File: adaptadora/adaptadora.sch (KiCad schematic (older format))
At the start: 27 parts, among them J1 Conn_Coaxial, J10 Conn_Coaxial, J11 Conn_Coaxial, J2 Conn_Coaxial, J3 Conn_Coaxial, J4 Conn_Coaxial, J5 Conn_02x20_Odd_Even, J6 Conn_01x02, J7 Conn_02x20_Odd_Even, J8 Conn_01x04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

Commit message: esq y pcb work in progress
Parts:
- added H1, H2, H3, H4, H5: MountingHole, MountingHole:MountingHole_3.2mm_M3_Pad, symbol Mechanical:MountingHole
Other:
- moved on the sheet: D1, D2, J1, J2, J3, J4, J7, JP1, JP2, R1, R2, RV1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

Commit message: mejorando BOM - work in progress
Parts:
- U25: Descripción (inglés) Dual 2.7-V High Slew Rate Rail-To-Rail Output Operational A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 -> General Purpose Amplifier 2 Circuit Rail-to-Rail 8-SOIC; Enlace https://www.digikey.com/product-detail/en/texas-instruments/TLV2772IDR/296-1902-1-ND/405014?utm_source=snapeda&utm_medium=aggregator&utm_campaign=symbol -> https://www.digikey.com/product-detail/en/texas-instruments/TLV2772IDR/296-1902-2-ND/374332; Número de Parte (Digi-Key) 296-1902-1-ND -> 296-1902-2-ND; Número de parte (Digi-Key) (none) -> 296-1902-2-ND
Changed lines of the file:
@@
 F 3 "http://www.ti.com/lit/ds/symlink/tlv2772.pdf" H 8950 1150 50  0001 L BNN
 F 4 "Texas Instruments" H 8950 1150 50  0001 L BNN "Fabricante"
-F 5 "Dual 2.7-V High Slew Rate Rail-To-Rail Output Operational Amplifier 8-SOIC -40 to 125" H 8950 1150 50  0001 L BNN "Descripción (inglés)"
-F 6 "296-1902-1-ND" H 8950 1150 50  0001 L BNN "Número de Parte (Digi-Key)"
-F 7 "https://www.digikey.com/product-detail/en/texas-instruments/TLV2772IDR/296-1902-1-ND/405014?utm_source=snapeda&utm_medium=aggregator&utm_campaign=symbol" H 8950 1150 50  0001 L BNN "Enlace"
+F 5 "General Purpose Amplifier 2 Circuit Rail-to-Rail 8-SOIC" H 8950 1150 50  0001 L BNN "Descripción (inglés)"
+F 6 "296-1902-2-ND" H 8950 1150 50  0001 L BNN "Número de Parte (Digi-Key)"
+F 7 "https://www.digikey.com/product-detail/en/texas-instruments/TLV2772IDR/296-1902-2-ND/374332" H 8950 1150 50  0001 L BNN "Enlace"
+F 8 "296-1902-2-ND" H 8950 1600 50  0001 C CNN "Número de parte (Digi-Key)"
+F 9 "" H 8950 1600 50  0001 C CNN "Campo9"
+F 10 "" H 8950 1600 50  0001 C CNN "Campo10"
 	1    8950 1600
 	1    0    0    -1
@@
 $EndComp
 $Comp
-L power:GND #PWR04
-U 1 1 5DAF1F2B
-P 5150 4950
-F 0 "#PWR04" H 5150 4700 50  0001 C CNN
-F 1 "GND" H 5155 4777 50  0000 C CNN
-F 2 "" H 5150 4950 50  0001 C CNN
-F 3 "" H 5150 4950 50  0001 C CNN
-	1    5150 4950
-	1    0    0    -1
-$EndComp
-$Comp
 L power:+5V #PWR05
 U 1 1 5DAF2B68
@@
 Wire Wire Line
 	5400 5100 5600 5100
-Text GLabel 5600 5300 0    50   Input ~ 0
-DAC_CLK
-Wire Wire Line
-	5000 5700 5600 5700
-Wire Wire Line
-	5000 5600 5600 5600
-Wire Wire Line
-	5000 5500 5600 5500
-Wire Wire Line
-	5000 5400 5600 5400
-Entry Wire Line
-	4900 5300 5000 5400
-Entry Wire Line
-	4900 5400 5000 5500
-Entry Wire Line
-	4900 5500 5000 5600
-Entry Wire Line
-	4900 5600 5000 5700
-Text Label 5000 5700 0    50   ~ 0
-DAC0
-Text Label 5000 5600 0    50   ~ 0
-DAC2
-Text Label 5000 5500 0    50   ~ 0
-DAC4
-Text Label 5000 5400 0    50   ~ 0
-DAC6
 Entry Wire Line
 	6650 5300 6750 5200
@@
 Wire Wire Line
 	1550 7150 2300 7150
+Text Label 5000 5400 0    50   ~ 0
+DAC6
+Text Label 5000 5500 0    50   ~ 0
+DAC4
+Text Label 5000 5600 0    50   ~ 0
+DAC2
+Text Label 5000 5700 0    50   ~ 0
+DAC0
+Entry Wire Line
+	4900 5600 5000 5700
+Entry Wire Line
+	4900 5500 5000 5600
+Entry Wire Line
+	4900 5400 5000 5500
+Entry Wire Line
+	4900 5300 5000 5400
+Wire Wire Line
+	5000 5400 5600 5400
+Wire Wire Line
+	5000 5500 5600 5500
+Wire Wire Line
+	5000 5600 5600 5600
+Wire Wire Line
+	5000 5700 5600 5700
+Text GLabel 5600 5300 0    50   Input ~ 0
+DAC_CLK
+$Comp
+L power:GND #PWR04
+U 1 1 5DAF1F2B
+P 5150 4950
+F 0 "#PWR04" H 5150 4700 50  0001 C CNN
+F 1 "GND" H 5155 4777 50  0000 C CNN
+F 2 "" H 5150 4950 50  0001 C CNN
+F 3 "" H 5150 4950 50  0001 C CNN
+	1    5150 4950
+	1    0    0    -1
+$EndComp
 Wire Bus Line
 	6750 4550 6750 5500

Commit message: se ordenan campos de integrados
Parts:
- C1, C2, C4, C5: value 0.1uF-50V -> 0_1uF-50V
- C3, C6, C7: value 2.2uF-35V -> 2_2uF-35V
- U25: Descripción (inglés) General Purpose Amplifier 2 Circuit Rail-to-Rail 8-SOIC -> Dual 2.7-V High Slew Rate Rail-To-Rail Output Operational A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; Número de parte (Digi-Key) 296-1902-2-ND -> (none)
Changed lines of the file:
@@
 F 3 "http://www.ti.com/lit/ds/symlink/tlv2772.pdf" H 8950 1150 50  0001 L BNN
 F 4 "Texas Instruments" H 8950 1150 50  0001 L BNN "Fabricante"
-F 5 "General Purpose Amplifier 2 Circuit Rail-to-Rail 8-SOIC" H 8950 1150 50  0001 L BNN "Descripción (inglés)"
+F 5 "Dual 2.7-V High Slew Rate Rail-To-Rail Output Operational Amplifier 8-SOIC -40 to 125" H 8950 1150 50  0001 L BNN "Descripción (inglés)"
 F 6 "296-1902-2-ND" H 8950 1150 50  0001 L BNN "Número de Parte (Digi-Key)"
 F 7 "https://www.digikey.com/product-detail/en/texas-instruments/TLV2772IDR/296-1902-2-ND/374332" H 8950 1150 50  0001 L BNN "Enlace"
-F 8 "296-1902-2-ND" H 8950 1600 50  0001 C CNN "Número de parte (Digi-Key)"
-F 9 "" H 8950 1600 50  0001 C CNN "Campo9"
-F 10 "" H 8950 1600 50  0001 C CNN "Campo10"
 	1    8950 1600
 	1    0    0    -1
@@
 P 8000 1400
 F 0 "C1" V 7748 1400 50  0000 C CNN
-F 1 "0.1uF-50V" V 7850 1300 50  0000 C CNN
+F 1 "0_1uF-50V" V 7850 1300 50  0000 C CNN
 F 2 "Capacitor_SMD:C_0805_2012Metric" H 8038 1250 50  0001 C CNN
 F 3 "~" H 8000 1400 50  0001 C CNN
@@
 P 10300 4950
 F 0 "C7" H 10415 4996 50  0000 L CNN
-F 1 "2.2uF-35V" H 10415 4905 50  0000 L CNN
+F 1 "2_2uF-35V" H 10415 4905 50  0000 L CNN
 F 2 "Capacitor_Tantalum_SMD:CP_EIA-6032-28_Kemet-C" H 10300 4950 50  0001 C CNN
 F 3 "~" H 10300 4950 50  0001 C CNN
@@
 P 10300 4150
 F 0 "C6" H 10415 4196 50  0000 L CNN
-F 1 "2.2uF-35V" H 10415 4105 50  0000 L CNN
+F 1 "2_2uF-35V" H 10415 4105 50  0000 L CNN
 F 2 "Capacitor_Tantalum_SMD:CP_EIA-6032-28_Kemet-C" H 10300 4150 50  0001 C CNN
 F 3 "~" H 10300 4150 50  0001 C CNN
@@
 P 9550 4950
 F 0 "C5" H 9665 4996 50  0000 L CNN
-F 1 "0.1uF-50V" H 9665 4905 50  0000 L CNN
+F 1 "0_1uF-50V" H 9665 4905 50  0000 L CNN
 F 2 "Capacitor_SMD:C_0805_2012Metric" H 9588 4800 50  0001 C CNN
 F 3 "~" H 9550 4950 50  0001 C CNN
@@
 P 9550 4150
 F 0 "C4" H 9665 4196 50  0000 L CNN
-F 1 "0.1uF-50V" H 9665 4105 50  0000 L CNN
+F 1 "0_1uF-50V" H 9665 4105 50  0000 L CNN
 F 2 "Capacitor_SMD:C_0805_2012Metric" H 9588 4000 50  0001 C CNN
 F 3 "~" H 9550 4150 50  0001 C CNN
@@
 P 9550 5800
 F 0 "C2" H 9665 5846 50  0000 L CNN
-F 1 "0.1uF-50V" H 9665 5755 50  0000 L CNN
+F 1 "0_1uF-50V" H 9665 5755 50  0000 L CNN
 F 2 "Capacitor_SMD:C_0805_2012Metric" H 9588 5650 50  0001 C CNN
 F 3 "~" H 9550 5800 50  0001 C CNN
@@
 P 10300 5800
 F 0 "C3" H 10415 5846 50  0000 L CNN
-F 1 "2.2uF-35V" H 10415 5755 50  0000 L CNN
+F 1 "2_2uF-35V" H 10415 5755 50  0000 L CNN
 F 2 "Capacitor_Tantalum_SMD:CP_EIA-6032-28_Kemet-C" H 10300 5800 50  0001 C CNN
 F 3 "~" H 10300 5800 50  0001 C CNN

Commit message: se cambia footprint de componentes y el posicionamiento
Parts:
- D1, D2: footprint Diode_SMD:D_0201_0603Metric -> Diode_THT:D_DO-15_P10.16mm_Horizontal
- JP1, JP2: footprint Jumper:SolderJumper-3_P1.3mm_Open_Pad1.0x1.5mm_NumberLabels -> Connector_PinHeader_2.54mm:PinHeader_1x03_P2.54mm_Vertical
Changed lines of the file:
@@
 F 0 "JP1" V 1754 5037 50  0000 L CNN
 F 1 "Jumper_3_Open" V 1845 5037 50  0000 L CNN
-F 2 "Jumper:SolderJumper-3_P1.3mm_Open_Pad1.0x1.5mm_NumberLabels" H 1800 4950 50  0001 C CNN
+F 2 "Connector_PinHeader_2.54mm:PinHeader_1x03_P2.54mm_Vertical" H 1800 4950 50  0001 C CNN
 F 3 "~" H 1800 4950 50  0001 C CNN
 	1    1800 4950
@@
 F 0 "D1" V 2754 5329 50  0000 L CNN
 F 1 "D_TVS" V 2845 5329 50  0000 L CNN
-F 2 "Diode_SMD:D_0201_0603Metric" H 2800 5250 50  0001 C CNN
+F 2 "Diode_THT:D_DO-15_P10.16mm_Horizontal" H 2800 5250 50  0001 C CNN
 F 3 "~" H 2800 5250 50  0001 C CNN
 	1    2800 5250
@@
 F 0 "JP2" V 1754 6637 50  0000 L CNN
 F 1 "Jumper_3_Open" V 1845 6637 50  0000 L CNN
-F 2 "Jumper:SolderJumper-3_P1.3mm_Open_Pad1.0x1.5mm_NumberLabels" H 1800 6550 50  0001 C CNN
+F 2 "Connector_PinHeader_2.54mm:PinHeader_1x03_P2.54mm_Vertical" H 1800 6550 50  0001 C CNN
 F 3 "~" H 1800 6550 50  0001 C CNN
 	1    1800 6550
@@
 F 0 "D2" V 2754 6929 50  0000 L CNN
 F 1 "D_TVS" V 2845 6929 50  0000 L CNN
-F 2 "Diode_SMD:D_0201_0603Metric" H 2800 6850 50  0001 C CNN
+F 2 "Diode_THT:D_DO-15_P10.16mm_Horizontal" H 2800 6850 50  0001 C CNN
 F 3 "~" H 2800 6850 50  0001 C CNN
 	1    2800 6850

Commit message: se quita el gpio 2x20 por un 2x6
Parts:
- removed J7: Conn_02x20_Odd_Even, Connector_PinHeader_2.00mm:PinHeader_2x20_P2.00mm_Vertical, symbol Connector_Generic:Conn_02x20_Odd_Even
- J5: value Conn_02x20_Odd_Even -> Conn_02x06_Odd_Even; footprint Connector_PinHeader_2.54mm:PinHeader_2x20_P2.54mm_Horizontal -> Connector_PinHeader_2.54mm:PinHeader_2x06_P2.54mm_Horizontal; symbol Connector_Generic:Conn_02x20_Odd_Even -> Connector_Generic:Conn_02x06_Odd_Even
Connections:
- net labels removed: DAC0, DAC1, DAC2, DAC3, DAC4, DAC5, DAC6, DAC7, DAC[7..0], DAC_CLK
- wire segments 147 -> 126
- no-connect marks 53 -> 6
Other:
- note removed: "DAC"
- moved on the sheet: C1, C2, C3, C4, C5, C6, C7, D1, D2, H1, H2, H3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

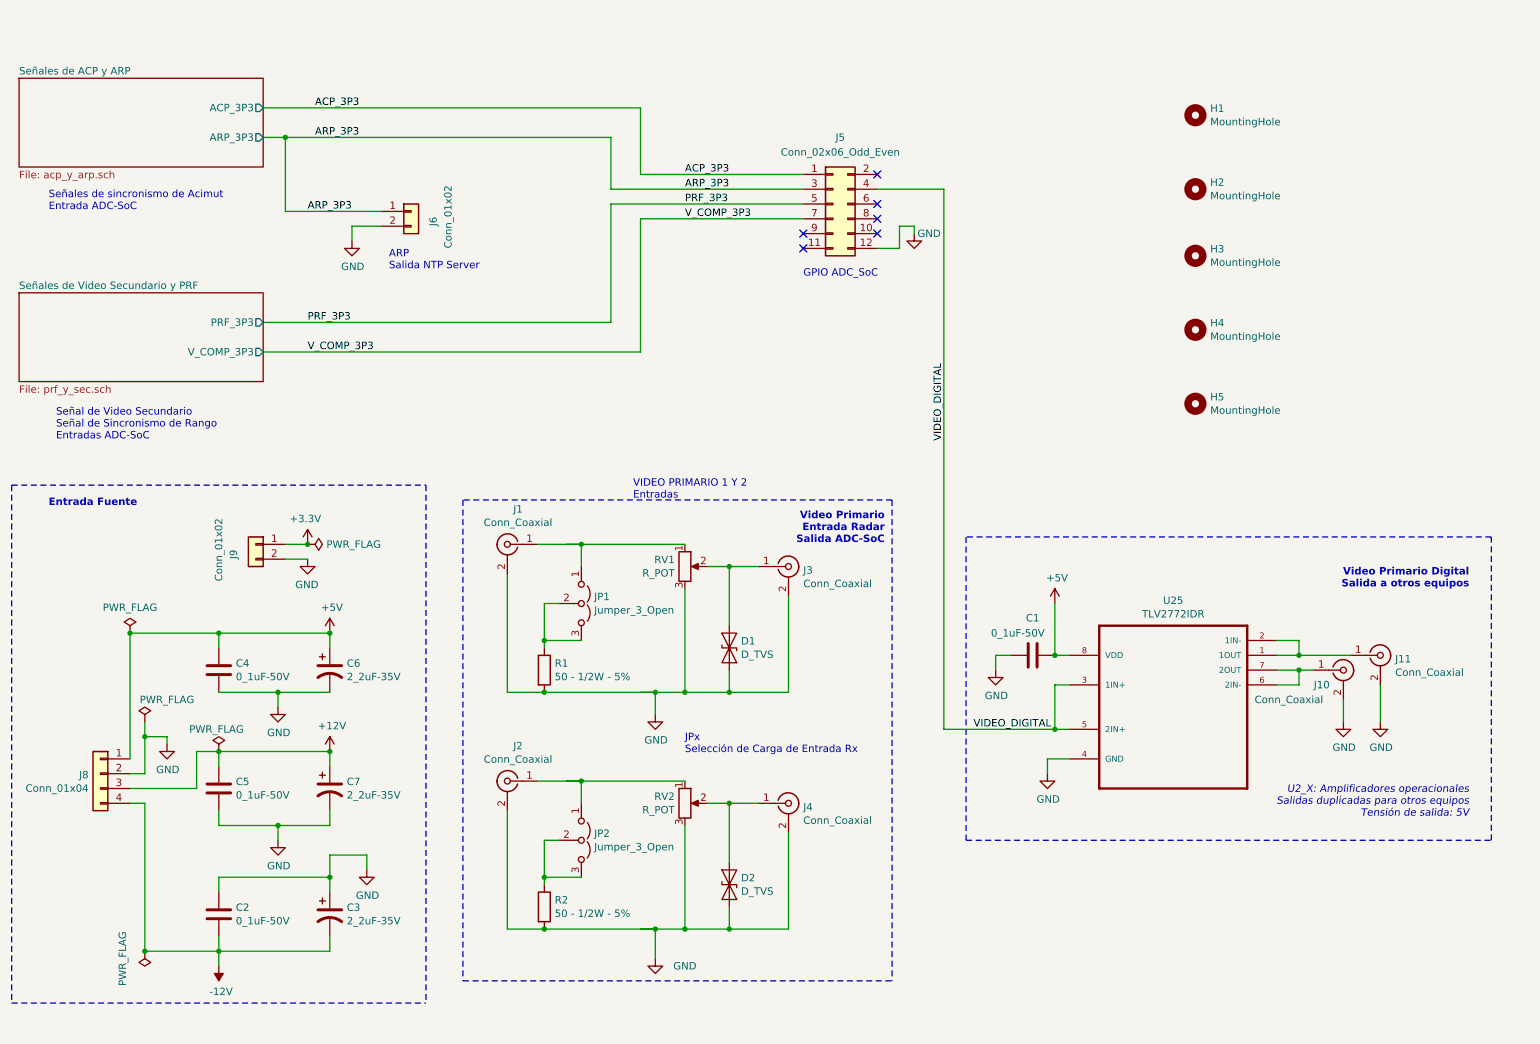
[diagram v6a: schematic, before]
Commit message: se agrega planos de tierra
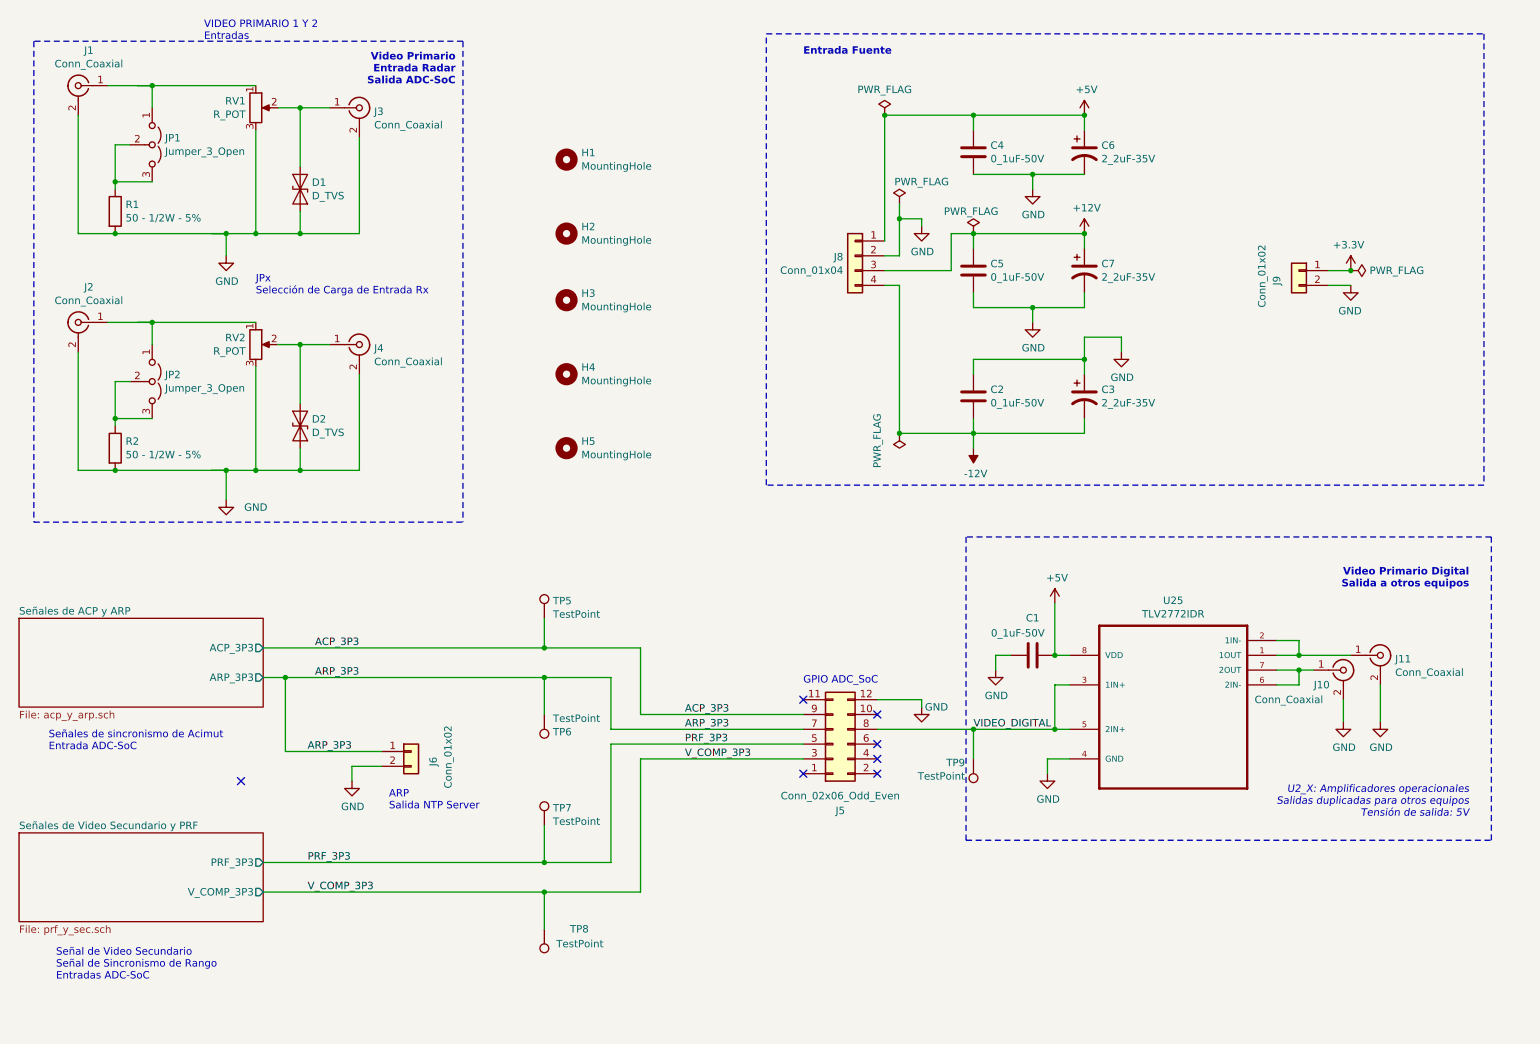
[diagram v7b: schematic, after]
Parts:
- added TP5, TP6, TP7, TP8, TP9: TestPoint, adaptadora:TestPoint_THTPad_1.5x1.5mm_Drill0.7mm, symbol Connector:TestPoint
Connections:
- wire segments 126 -> 132
- no-connect marks 6 -> 7
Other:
- moved on the sheet: C2, C3, C4, C5, C6, C7, D1, D2, H1, H2, H3, H4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
